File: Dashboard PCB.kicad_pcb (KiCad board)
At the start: 2 copper layers, 150 x 100.2 mm, 74 parts, among them J1 Controls_Leader_Export_02x06, J3 INDICATOR_SWITCH_OUT, J5 Horn_In_01x02, J6 Horn_Out_01x02, J8 Supp_Out, J9 Supp_In, Q1 TO200P800X182-5N, Q2 Q_PMOS_GDS

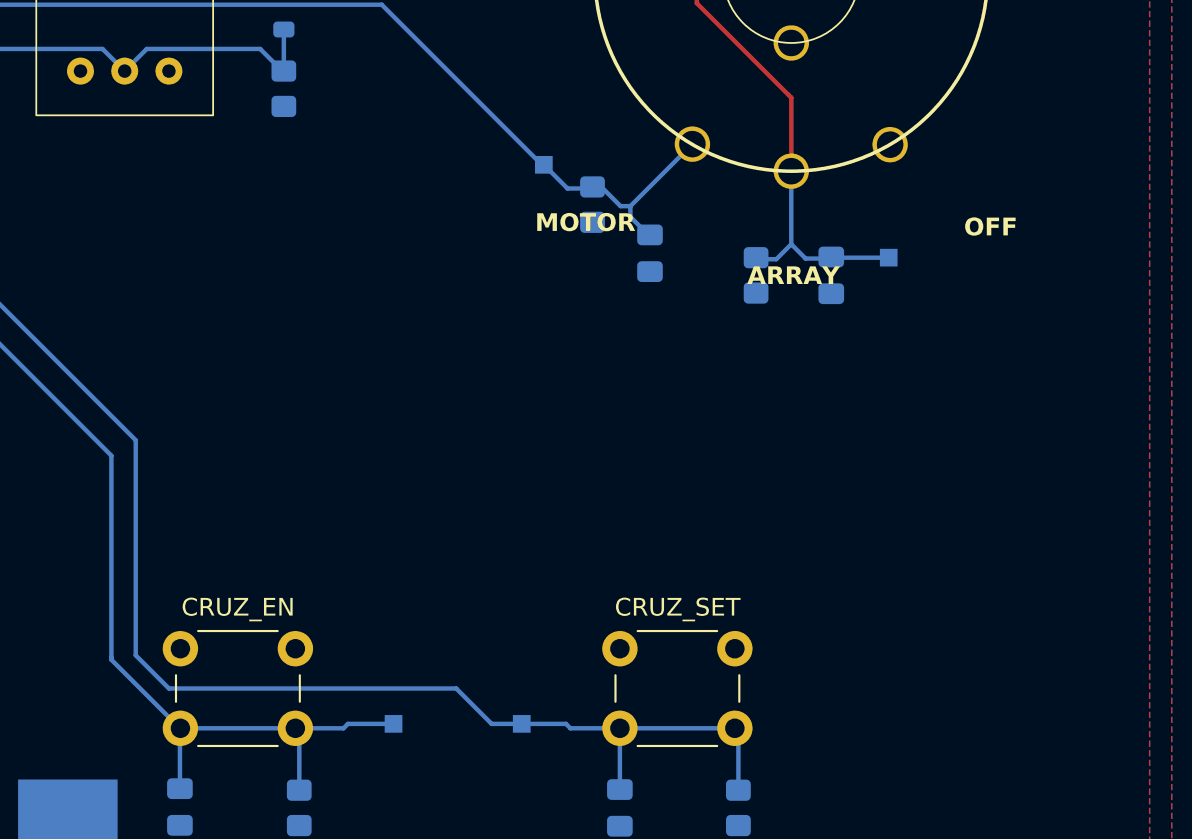
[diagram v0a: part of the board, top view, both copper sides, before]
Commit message: make ign off cruz en or some shit
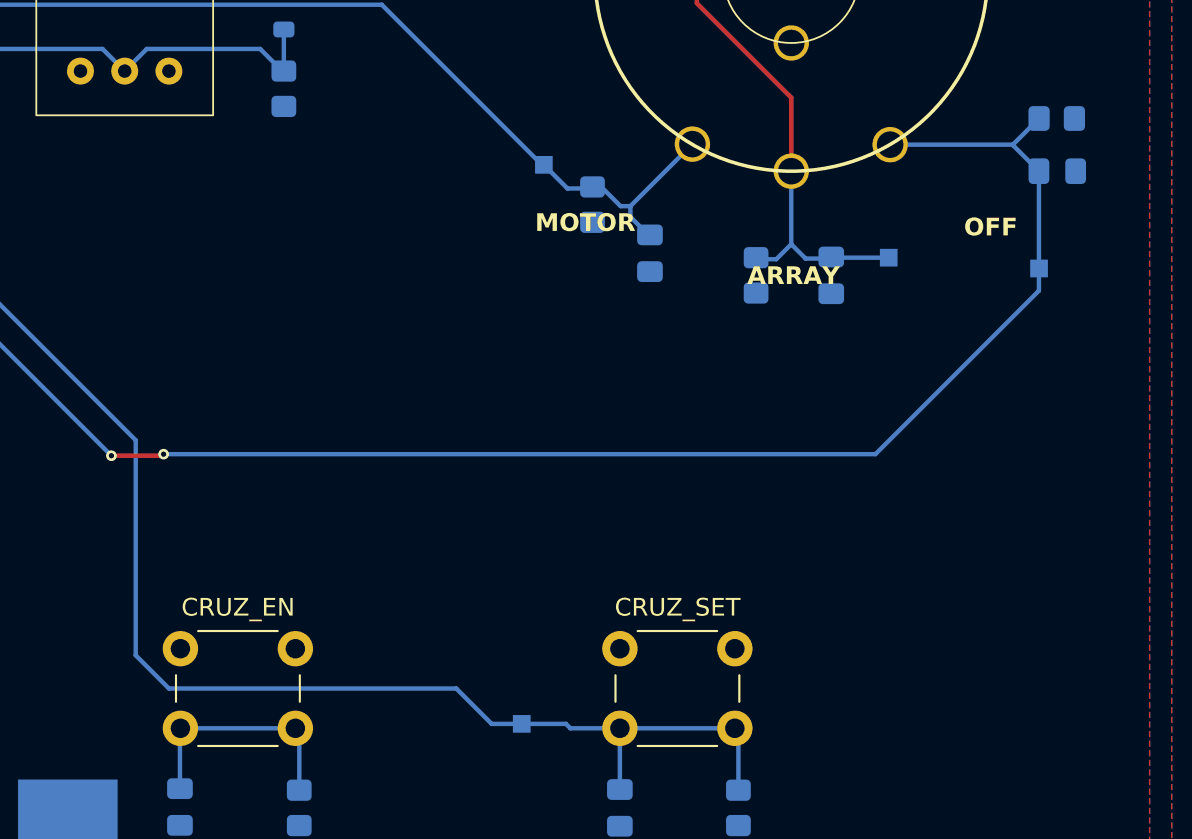
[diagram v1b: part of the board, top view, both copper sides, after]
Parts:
- added C12: 5uF, Capacitor_SMD:C_0805_2012Metric_Pad1.18x1.45mm_HandSolder, B.Cu at (189.8, 93.5)
- added R19: 10k, Resistor_SMD:R_0805_2012Metric_Pad1.20x1.40mm_HandSolder, B.Cu at (189.8, 90.5)
- moved IGN_OFF 44.7 mm to (188.8, 99.0)
- moved G*** 2.51 mm to (155.5, 107.0)
- renumbered CRUZ_EN to IGN_OFF, SUPP+1 to SUPP+, SUPP-1 to SUPP-
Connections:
- C9 pad 1: /CRUZ_EN -> unconnected-(C9-Pad1)
- CRUZ_EN_SW1 pad 2: /CRUZ_EN -> unconnected-(C9-Pad1)
- IGN_SW1 pad 4: unconnected-(IGN_SW1-Pad4) -> /CRUZ_EN
- R9 pad 2: /CRUZ_EN -> unconnected-(C9-Pad1)
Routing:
- net /CRUZ_EN: track 96.5 -> 133.8 mm, vias 0 -> 2
- net unconnected-(C9-Pad1): track 0.00 -> 14.3 mm
